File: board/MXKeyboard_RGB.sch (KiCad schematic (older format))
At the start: 2 parts

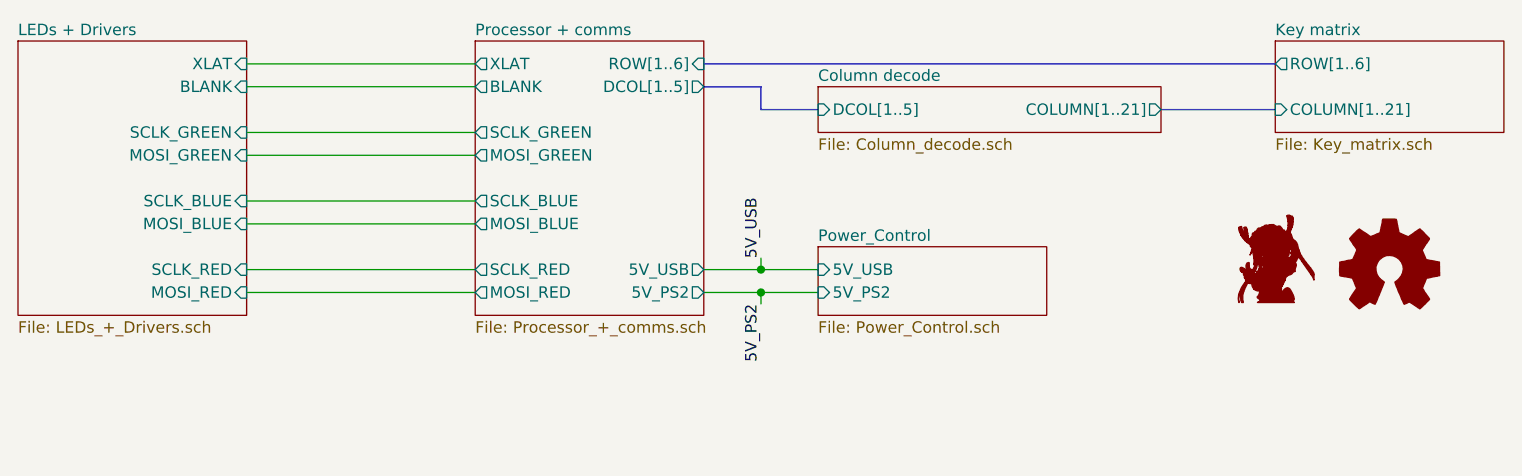
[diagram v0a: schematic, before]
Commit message: Further cleanup and added footprints for SPI termination resistors for the LED drivers as a Just In Case
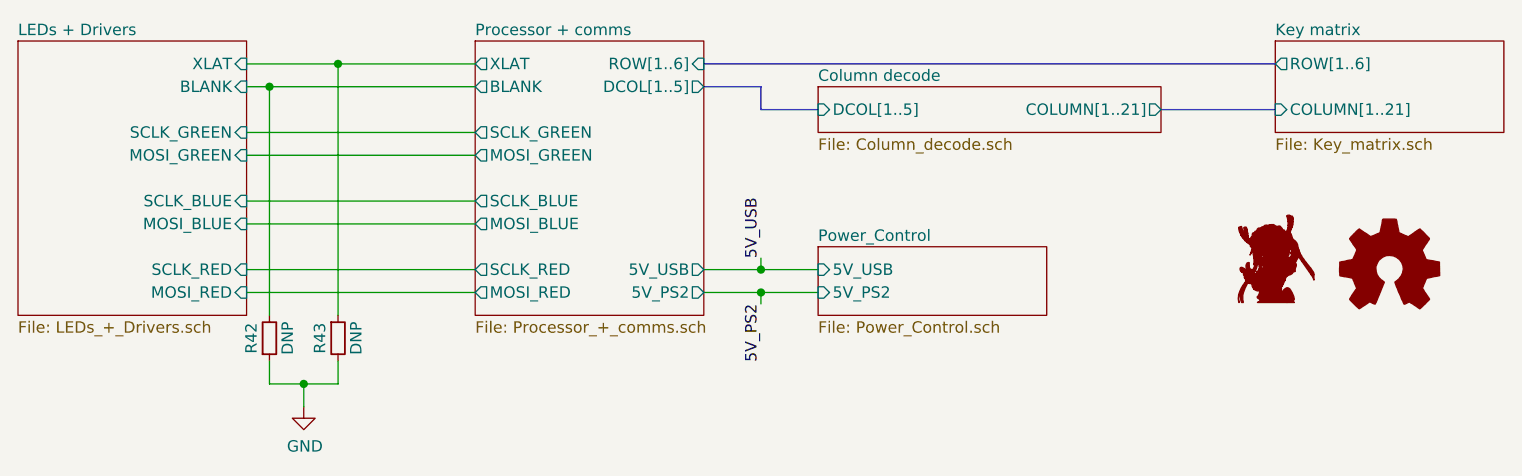
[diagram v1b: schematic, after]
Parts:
- added R42, R43: DNP, rhais_rcl:R0603, symbol Device:R_Small
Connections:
- net LEDs + Drivers/BLANK: now also R42.2
- net LEDs + Drivers/XLAT: now also R43.1
- new net GND: R42.1, R43.2
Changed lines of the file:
@@
 $EndSheet
 Wire Wire Line
-	3500 3600 4500 3600
+	3500 3600 3900 3600
 Wire Wire Line
-	4500 3700 3500 3700
+	4500 3700 3600 3700
 Wire Wire Line
 	3500 3900 4500 3900
@@
 	1    0    0    -1
 $EndComp
+$Comp
+L Device:R_Small R42
+U 1 1 61B40AAF
+P 3600 4800
+F 0 "R42" V 3550 4800 50  0000 C BNN
+F 1 "DNP" V 3650 4800 50  0000 C TNN
+F 2 "rhais_rcl:R0603" H 3600 4800 50  0001 C CNN
+F 3 "~" H 3600 4800 50  0001 C CNN
+	1    3600 4800
+	1    0    0    1
+$EndComp
+$Comp
+L Device:R_Small R43
+U 1 1 61B416B1
+P 3900 4800
+F 0 "R43" V 3850 4800 50  0000 C BNN
+F 1 "DNP" V 3950 4800 50  0000 C TNN
+F 2 "rhais_rcl:R0603" H 3900 4800 50  0001 C CNN
+F 3 "~" H 3900 4800 50  0001 C CNN
+	1    3900 4800
+	1    0    0    -1
+$EndComp
+Wire Wire Line
+	3600 4900 3600 5000
+Wire Wire Line
+	3600 5000 3750 5000
+Wire Wire Line
+	3900 5000 3900 4900
+Wire Wire Line
+	3750 5000 3750 5100
+Connection ~ 3750 5000
+Wire Wire Line
+	3750 5000 3900 5000
+$Comp
+L power:GND #PWR070
+U 1 1 61B42470
+P 3750 5100
+F 0 "#PWR070" H 3750 4850 50  0001 C CNN
+F 1 "GND" H 3755 4927 50  0000 C CNN
+F 2 "" H 3750 5100 50  0001 C CNN
+F 3 "" H 3750 5100 50  0001 C CNN
+	1    3750 5100
+	1    0    0    -1
+$EndComp
+Wire Wire Line
+	3600 4700 3600 3700
+Connection ~ 3600 3700
+Wire Wire Line
+	3600 3700 3500 3700
+Wire Wire Line
+	3900 4700 3900 3600
+Connection ~ 3900 3600
+Wire Wire Line
+	3900 3600 4500 3600
 $EndSCHEMATC
